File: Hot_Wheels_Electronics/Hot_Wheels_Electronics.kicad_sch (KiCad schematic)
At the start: 19 parts, among them J1 motor_output_a, J2 motor_output_b, M1 motor_driver: DRV8833PW, SW1 main_switch, U1 esp32-wemos-d1-mini, U3 BMI160, U4 QITN BEC

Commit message: Adrian’s PCB Schematic development (#33)
* migrated to bare castellated module and used safe gpio pins

* worked on programmer

---------

Co-authored-by: Adrian <adrian@Adrians-MacBook-Neo.local>
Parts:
- added J3: Conn_02x05_Socket, Connector_RJ:RJ45_Abracon_ARJP11A-MA_Horizontal, symbol Connector_Generic:Conn_02x05_Counter_Clockwise
- added U2: ESP32-WROOM-32, RF_Module:ESP32-WROOM-32, symbol RF_Module:ESP32-WROOM-32
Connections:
- net +3V3: now also U2.2 (VDD)
- net GND: now also J3.4 (Pin_4), J3.5 (Pin_5), U2.1 (GND), U2.15 (GND), U2.38 (GND), U2.39 (GND)
- net drv_curr_a: now also U2.6 (IO34)
- net drv_curr_b: now also U2.7 (IO35)
- net drv_input_a1: now also U2.10 (IO25)
- net drv_input_a2: now also U2.11 (IO26)
- net drv_input_b1: now also U2.12 (IO27)
- net drv_input_b2: now also U2.13 (IO14)
- net i2c_scl: now also U2.36 (IO22)
- net i2c_sda: now also U2.33 (IO21)
- net imu_cs: now also U2.28 (IO17)
- net imu_miso: now also U2.31 (IO19)
- net imu_mosi: now also U2.37 (IO23)
- net imu_sck: now also U2.30 (IO18)
- net servo_signal: now also U2.9 (IO33)
- new net battery_voltage_sense: U2.4 (SENSOR_VP)
- new net drv_nfault: U2.26 (IO4)
- new net drv_nsleep: U2.16 (IO13)
- new net esp_boot: U2.25 (IO0)
- new net esp_reset: U2.3 (EN)
- new net imu_int1: U2.27 (IO16)
- new net motor_temp: U2.5 (SENSOR_VN)
- new net uart_rx: J3.8 (Pin_8), U2.34 (RXD0/IO3)
- new net uart_tx: J3.7 (Pin_7), U2.35 (TXD0/IO1)
- new net wheel_speed: U2.8 (IO32)
- no-connect marks 0 -> 10
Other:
- moved on the sheet: C1, C2, C3, C4, C6, J1, J2, M1, R1, R2, R3, R4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

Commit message: finalised programming interface pinout
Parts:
- removed J3: Conn_02x05_Socket, Connector_RJ:RJ45_Abracon_ARJP11A-MA_Horizontal, symbol Connector_Generic:Conn_02x05_Counter_Clockwise
- added J3: Conn_01x05_Socket, symbol Connector:Conn_01x05_Socket
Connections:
- net GND: now also J3.1 (Pin_1)
- net esp_boot: now also J3.4 (Pin_4)
- net esp_reset: now also J3.5 (Pin_5)
- net uart_rx: now also J3.2 (Pin_2)
- net uart_tx: now also J3.3 (Pin_3)
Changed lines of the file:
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@@
 	(text_box "programming interface"
 		(exclude_from_sim no)
-		(at 326.39 63.5 0)
-		(size 68.58 76.2)
+		(at 326.39 77.47 0)
+		(size 68.58 31.75)
 		(margins 0.9525 0.9525 0.9525 0.9525)
 		(stroke
@@
 	)
 	(junction
-		(at 358.14 100.33)
-		(diameter 0)
-		(color 0 0 0 0)
-	)
-	(junction
 		(at 129.54 121.92)
 		(diameter 0)
@@
 	(wire
 		(pts
+			(xy 350.52 88.9) (xy 350.52 100.33)
+		)
+		(stroke
+			(width 0)
+			(type default)
+		)
+	)
+	(wire
+		(pts
+			(xy 368.3 88.9) (xy 350.52 88.9)
+		)
+		(stroke
+			(width 0)
+			(type default)
+		)
+	)
+	(wire
+		(pts
 			(xy 118.11 63.5) (xy 138.43 63.5)
 		)
@@
 	(wire
 		(pts
+			(xy 358.14 91.44) (xy 358.14 100.33)
+		)
+		(stroke
+			(width 0)
+			(type default)
+		)
+	)
+	(wire
+		(pts
 			(xy 165.1 30.48) (xy 170.18 30.48)
 		)
@@
 	(wire
 		(pts
+			(xy 336.55 83.82) (xy 336.55 97.79)
+		)
+		(stroke
+			(width 0)
+			(type default)
+		)
+	)
+	(wire
+		(pts
 			(xy 271.78 125.73) (xy 267.97 125.73)
 		)
@@
 	(wire
 		(pts
+			(xy 341.63 86.36) (xy 341.63 100.33)
+		)
+		(stroke
+			(width 0)
+			(type default)
+		)
+	)
+	(wire
+		(pts
 			(xy 214.63 87.63) (xy 237.49 87.63)
 		)
@@
 	(wire
 		(pts
+			(xy 368.3 83.82) (xy 336.55 83.82)
+		)
+		(stroke
+			(width 0)
+			(type default)
+		)
+	)
+	(wire
+		(pts
 			(xy 59.69 135.89) (xy 109.22 135.89)
 		)
@@
 	(wire
 		(pts
+			(xy 368.3 93.98) (xy 368.3 100.33)
+		)
+		(stroke
+			(width 0)
+			(type default)
+		)
+	)
+	(wire
+		(pts
 			(xy 53.34 167.64) (xy 53.34 166.37)
 		)
@@
 	(wire
 		(pts
-			(xy 134.62 151.13) (xy 153.67 151.13)
+			(xy 368.3 86.36) (xy 341.63 86.36)
 		)
 		(stroke
@@
 	(wire
 		(pts
-			(xy 118.11 81.28) (xy 138.43 81.28)
+			(xy 134.62 151.13) (xy 153.67 151.13)
 		)
 		(stroke
@@
 	(wire
 		(pts
-			(xy 214.63 80.01) (xy 237.49 80.01)
+			(xy 118.11 81.28) (xy 138.43 81.28)
 		)
 		(stroke
@@
 	(wire
 		(pts
-			(xy 358.14 97.79) (xy 358.14 100.33)
+			(xy 214.63 80.01) (xy 237.49 80.01)
 		)
 		(stroke
@@
 		)
 	)
+	(wire
+		(pts
+			(xy 368.3 91.44) (xy 358.14 91.44)
+		)
+		(stroke
+			(width 0)
+			(type default)
+		)
+	)
 	(label "uart_rx"
-		(at 370.84 95.25 0)
+		(at 341.63 100.33 0)
 		(effects
 			(font
@@
 	)
 	(label "uart_tx"
-		(at 370.84 97.79 0)
+		(at 350.52 100.33 0)
 		(effects
 			(font
@@
 	)
 	(label "esp_reset"
-		(at 347.98 80.01 0)
+		(at 368.3 100.33 0)
 		(effects
 			(font
@@
 	)
 	(label "esp_boot"
-		(at 367.03 77.47 0)
+		(at 358.14 100.33 0)
 		(effects
 			(font
@@
 	)
 	(symbol
+		(lib_id "Connector:Conn_01x05_Socket")
+		(at 373.38 88.9 0)
+		(unit 1)
+		(body_style 1)
+		(exclude_from_sim no)
+		(in_bom yes)
+		(on_board yes)
+		(in_pos_files yes)
+		(dnp no)
+		(fields_autoplaced yes)
+		(property "Reference" "J3"
+			(at 374.65 87.6299 0)
+			(show_name no)
+			(do_not_autoplace no)
+			(effects
+				(font
+					(size 1.27 1.27)
+				)
+				(justify left)
+			)
+		)
+		(property "Value" "Conn_01x05_Socket"
+			(at 374.65 90.1699 0)
+			(show_name no)
+			(do_not_autoplace no)
+			(effects
+				(font
+					(size 1.27 1.27)
+				)
+				(justify left)
+			)
+		)
+		(property "Footprint" ""
+			(at 373.38 88.9 0)
+			(hide yes)
+			(show_name no)
+			(do_not_autoplace no)
+			(effects
+				(font
+					(size 1.27 1.27)
+				)
+			)
+		)
+		(property "Datasheet" ""
+			(at 373.38 88.9 0)
+			(hide yes)
+			(show_name no)
+			(do_not_autoplace no)
+			(effects
+				(font
+					(size 1.27 1.27)
+				)
+			)
+		)
+		(property "Description" "Generic connector, single row, 01x05, script generated"
+			(at 373.38 88.9 0)
+			(hide yes)
+			(show_name no)
+			(do_not_autoplace no)
+			(effects
+				(font
+					(size 1.27 1.27)
+				)
+			)
+		)
+		(pin "1"
+		)
+		(pin "4"
+		)
+		(pin "3"
+		)
+		(pin "2"
+		)
+		(pin "5"
+		)
+		(instances
+			(project "Hot_Wheels_Electronics"
+				(path "/753fef37-370a-4893-8adb-358cd7fc1669"
+					(reference "J3")
+					(unit 1)
+				)
+			)
+		)
+	)
+	(symbol
 		(lib_id "Device:C")
 		(at 162.56 125.73 0)
@@
 	)
 	(symbol
-		(lib_id "Connector_Generic:Conn_02x05_Counter_Clockwise")
-		(at 363.22 95.25 0)
-		(unit 1)
-		(body_style 1)
-		(exclude_from_sim no)
-		(in_bom yes)
-		(on_board yes)
-		(in_pos_files yes)
-		(dnp no)
-		(property "Reference" "J3"
-			(at 364.49 104.902 0)
-			(show_name no)
-			(do_not_autoplace no)
-			(effects
-				(font
-					(size 1.27 1.27)
-				)
-				(justify left)
-			)
-		)
-		(property "Value" "Conn_02x05_Socket"
-			(at 364.236 103.124 0)
-			(show_name no)
-			(do_not_autoplace no)
-			(effects
-				(font
-					(size 1.27 1.27)
-				)
-				(justify left)
-			)
-		)
-		(property "Footprint" "Connector_RJ:RJ45_Abracon_ARJP11A-MA_Horizontal"
-			(at 363.22 95.25 0)
-			(hide yes)
-			(show_name no)
-			(do_not_autoplace no)
-			(effects
-				(font
-					(size 1.27 1.27)
-				)
-			)
-		)
-		(property "Datasheet" ""
-			(at 363.22 95.25 0)
-			(hide yes)
-			(show_name no)
-			(do_not_autoplace no)
-			(effects
-				(font
-					(size 1.27 1.27)
-				)
-			)
-		)
-		(property "Description" "Generic connector, double row, 02x05, counter clockwise pin numbering scheme (similar to DIP package numbering), script generated (kicad-library-utils/schlib/autogen/connector/)"
-			(at 363.22 95.25 0)
-			(hide yes)
-			(show_name no)
-			(do_not_autoplace no)
-			(effects
-				(font
-					(size 1.27 1.27)
-				)
-			)
-		)
-		(pin "3"
-		)
-		(pin "2"
-		)
-		(pin "4"
-		)
-		(pin "5"
-		)
-		(pin "1"
-		)
-		(pin "7"
-		)
-		(pin "10"
-		)
-		(pin "6"
-		)
-		(pin "8"
-		)
-		(pin "9"
-		)
-		(instances
-			(project "Hot_Wheels_Electronics"
-				(path "/753fef37-370a-4893-8adb-358cd7fc1669"
-					(reference "J3")
-					(unit 1)
-				)
-			)
-		)
-	)
-	(symbol
 		(lib_id "esp32-wemos-d1-mini:esp32-wemos-d1-mini")
 		(at 151.13 25.4 0)
@@
 	(symbol
 		(lib_id "power:GND")
-		(at 358.14 100.33 0)
+		(at 336.55 97.79 0)
 		(unit 1)
 		(body_style 1)
@@
 		(fields_autoplaced yes)
 		(property "Reference" "#PWR024"
-			(at 358.14 106.68 0)
+			(at 336.55 104.14 0)
 			(hide yes)
 			(show_name no)
@@
 		)
 		(property "Value" "GND"
-			(at 358.14 105.41 0)
+			(at 336.55 102.87 0)
 			(show_name no)
 			(do_not_autoplace no)
@@
 		)
 		(property "Footprint" ""
-			(at 358.14 100.33 0)
+			(at 336.55 97.79 0)
 			(hide yes)
 			(show_name no)
@@
 		)
 		(property "Datasheet" ""
-			(at 358.14 100.33 0)
+			(at 336.55 97.79 0)
 			(hide yes)
 			(show_name no)
@@
 		)
 		(property "Description" "Power symbol creates a global label with name \"GND\" , ground"
-			(at 358.14 100.33 0)
+			(at 336.55 97.79 0)
 			(hide yes)
 			(show_name no)

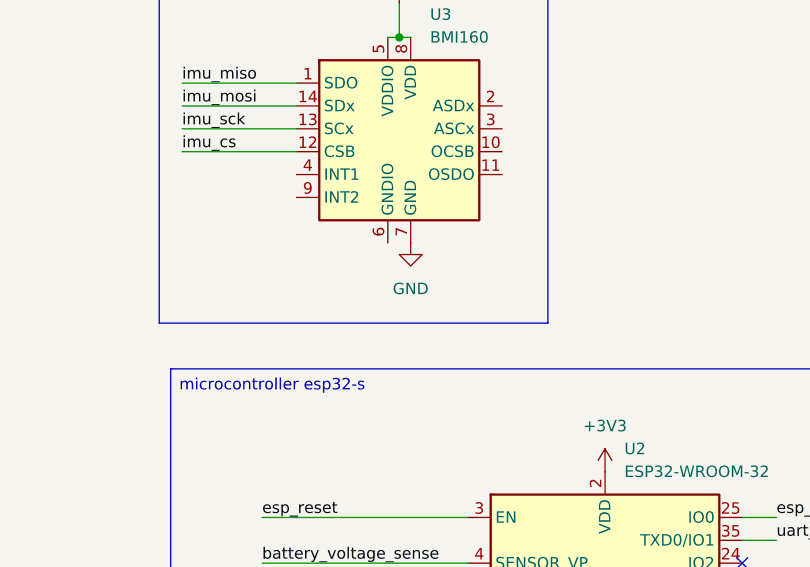
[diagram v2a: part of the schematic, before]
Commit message: correct gndio to gnd for bmi160
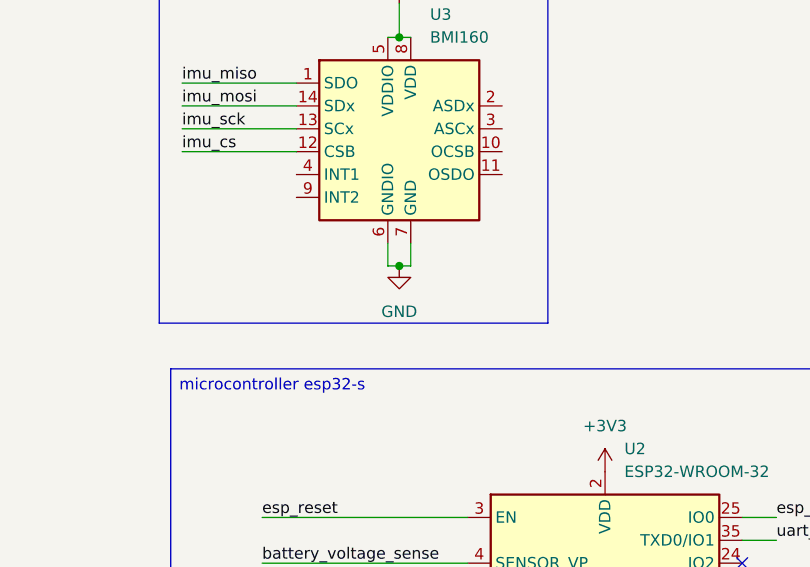
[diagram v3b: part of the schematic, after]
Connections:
- net GND: now also U3.6 (GNDIO)
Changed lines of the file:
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@@
 	)
 	(junction
+		(at 229.87 52.07)
+		(diameter 0)
+		(color 0 0 0 0)
+	)
+	(junction
 		(at 129.54 121.92)
 		(diameter 0)
@@
 	(wire
 		(pts
+			(xy 229.87 52.07) (xy 231.14 52.07)
+		)
+		(stroke
+			(width 0)
+			(type default)
+		)
+	)
+	(wire
+		(pts
 			(xy 271.78 133.35) (xy 267.97 133.35)
 		)
@@
 	(wire
 		(pts
+			(xy 228.6 52.07) (xy 229.87 52.07)
+		)
+		(stroke
+			(width 0)
+			(type default)
+		)
+	)
+	(wire
+		(pts
 			(xy 271.78 107.95) (xy 267.97 107.95)
 		)
@@
 	(wire
 		(pts
+			(xy 228.6 49.53) (xy 228.6 52.07)
+		)
+		(stroke
+			(width 0)
+			(type default)
+		)
+	)
+	(wire
+		(pts
 			(xy 134.62 151.13) (xy 153.67 151.13)
 		)
@@
 	(wire
 		(pts
+			(xy 231.14 52.07) (xy 231.14 49.53)
+		)
+		(stroke
+			(width 0)
+			(type default)
+		)
+	)
+	(wire
+		(pts
 			(xy 214.63 80.01) (xy 237.49 80.01)
 		)
@@
 	(symbol
 		(lib_id "power:GND")
-		(at 231.14 49.53 0)
+		(at 229.87 52.07 0)
 		(unit 1)
 		(body_style 1)
@@
 		(fields_autoplaced yes)
 		(property "Reference" "#PWR019"
-			(at 231.14 55.88 0)
+			(at 229.87 58.42 0)
 			(hide yes)
 			(show_name no)
@@
 		)
 		(property "Value" "GND"
-			(at 231.14 54.61 0)
+			(at 229.87 57.15 0)
 			(show_name no)
 			(do_not_autoplace no)
@@
 		)
 		(property "Footprint" ""
-			(at 231.14 49.53 0)
+			(at 229.87 52.07 0)
 			(hide yes)
 			(show_name no)
@@
 		)
 		(property "Datasheet" ""
-			(at 231.14 49.53 0)
+			(at 229.87 52.07 0)
 			(hide yes)
 			(show_name no)
@@
 		)
 		(property "Description" "Power symbol creates a global label with name \"GND\" , ground"
-			(at 231.14 49.53 0)
+			(at 229.87 52.07 0)
 			(hide yes)
 			(show_name no)
@@
 	)
 	(group ""
-		(members "01aca0a5-6109-4ce5-9355-7b87f4601e74" "09a08a93-8683-443f-8b29-de3845f97932"
-			"2dc8ba58-b076-46c3-a87f-543b95fdac97" "3447b82b-b97b-43af-b96f-6e21590b7fe5"
-			"3c698df9-5ee5-45d0-9333-f032ab9b243e" "56987a5d-d6a9-4c3d-b6bd-b1c7b62d0175"
-			"5c8158d2-1537-4e94-a4fb-e485d6d2c50a" "60f94aa7-73c1-4236-89b3-e49b53b76aef"
-			"625f0615-04b8-4763-992d-0324ef2ead93" "6b7e46e4-e696-4dd0-b8b5-77555a551b9e"
-			"7843d9bf-f7c6-41e4-a3f9-2de5ce7bfc5c" "870ef756-0600-4030-8520-4803448165f2"
-			"88b869df-24c0-4598-be50-ce491f43fd97" "8f7d1760-bc0e-40f8-a86a-d92ca4e2a77a"
-			"912a4eeb-b9ad-456e-ae5e-ee6a94d3d1a3" "a278264c-2ba2-4852-ba92-d82a899408cc"
+		(members "01aca0a5-6109-4ce5-9355-7b87f4601e74" "02fa4680-d0da-4db7-9a98-11e60b593739"
+			"09a08a93-8683-443f-8b29-de3845f97932" "2dc8ba58-b076-46c3-a87f-543b95fdac97"
+			"3447b82b-b97b-43af-b96f-6e21590b7fe5" "3c698df9-5ee5-45d0-9333-f032ab9b243e"
+			"492db433-0977-421f-b35a-1dcfc0d61f69" "56987a5d-d6a9-4c3d-b6bd-b1c7b62d0175"
+			"5aaceed6-2282-462d-9830-02043de01d8f" "5c8158d2-1537-4e94-a4fb-e485d6d2c50a"
+			"60f94aa7-73c1-4236-89b3-e49b53b76aef" "625f0615-04b8-4763-992d-0324ef2ead93"
+			"6b7e46e4-e696-4dd0-b8b5-77555a551b9e" "7843d9bf-f7c6-41e4-a3f9-2de5ce7bfc5c"
+			"870ef756-0600-4030-8520-4803448165f2" "88b869df-24c0-4598-be50-ce491f43fd97"
+			"8f7d1760-bc0e-40f8-a86a-d92ca4e2a77a" "912a4eeb-b9ad-456e-ae5e-ee6a94d3d1a3"
+			"a278264c-2ba2-4852-ba92-d82a899408cc" "cfaaa0c9-e082-4fe7-9f60-a525f73eb591"
+			"d447da89-7eb9-43d0-896b-e4271f2dba2d"
 		)
 	)

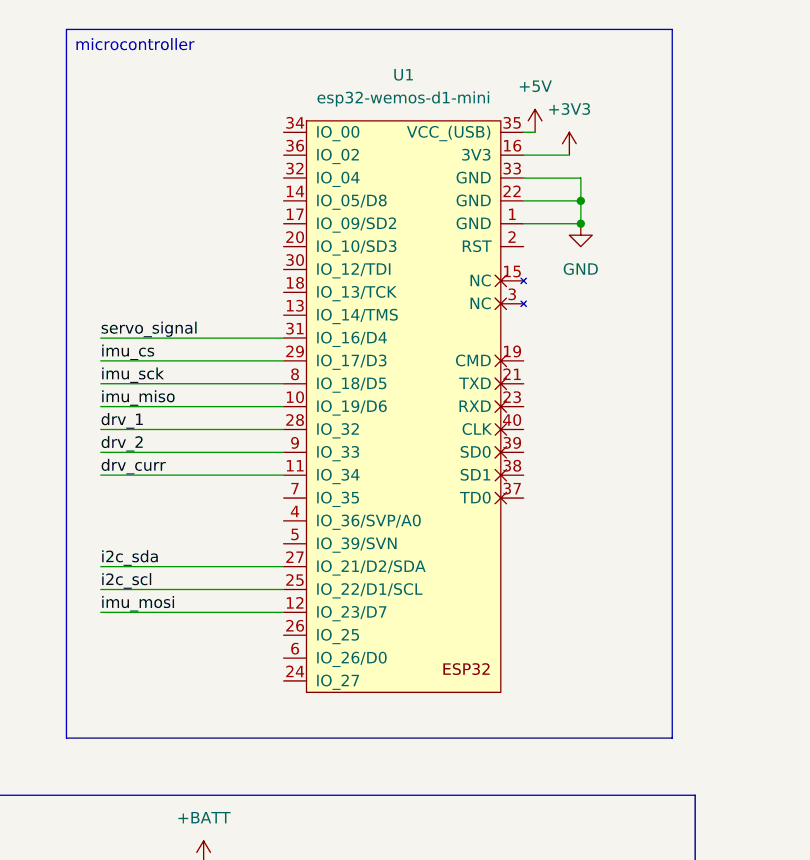
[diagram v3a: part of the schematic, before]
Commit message: placed do not place flag on old pcb mcu
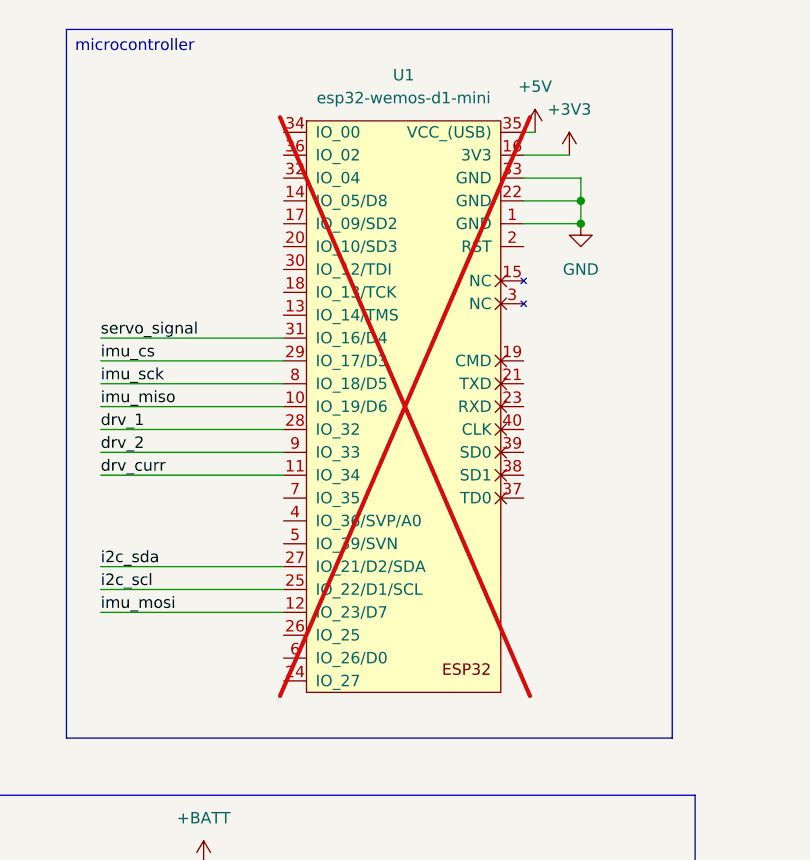
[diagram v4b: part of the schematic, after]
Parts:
- U1: now not fitted
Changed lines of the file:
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@@
 		(on_board yes)
 		(in_pos_files yes)
-		(dnp no)
+		(dnp yes)
 		(fields_autoplaced yes)
 		(property "Reference" "U1"
